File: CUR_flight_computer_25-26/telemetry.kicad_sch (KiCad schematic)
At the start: 10 parts, among them U4 Ai-Thinker-Ra-01, U9 E22-400M30S

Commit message: Update telemetry.kicad_sch
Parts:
- removed AE1: Antenna, symbol Device:Antenna
- removed C14: 100nF, symbol Device:C_Small
- removed C15: 10uF, symbol Device:C_Small
- removed C17, C18: C_Small, symbol Device:C_Small
- removed D1: D_Zener, symbol Device:D_Zener
- removed R7: 0, symbol Device:R_Small_US
- removed R8: 10k, symbol Device:R_Small_US
- removed U4: Ai-Thinker-Ra-01, RF_Module:Ai-Thinker-Ra-01-LoRa, symbol RF_Module:Ai-Thinker-Ra-01
- added AE2: Antenna, symbol Device:Antenna
- added C33: 1u, symbol Device:C_Small
- added C35, C36: C_Small, symbol Device:C_Small
- added R42: 0, symbol Device:R_Small_US
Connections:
- net VCC is gone; now on net +3V3: U9.10 (VCC), U9.9 (VCC)
- net +3V3: now also C33.1
- net GND: now also C33.2, C35.2, C36.2
- net RF_BUSY: now also U9.14 (BUSY)
- net RF_IO1: now also U9.13 (DIO1)
- net RF_IO2: now also U9.8 (DIO2)
- net RF_MISO: now also U9.16 (MISO)
- net RF_MOSI: now also U9.17 (MOSI)
- net RF_RXEN: now also U9.6 (RXEN)
- net RF_SCK: now also U9.18 (SCK)
- net RF_TXEN: now also U9.7 (TXEN)
- net ~{RF_NSS}: now also U9.19 (NSS)
- net ~{RF_RESET}: now also U9.15 (NRST)
- net at U9.21 (ANT): now also C35.1, R42.2
- new net: AE2.1 (A), C36.1, R42.1
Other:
- note added: "DIO1 - interrupt DIO2 - tx switch"
- note added: "Pick capacitor values to PI match antenna - leave to test later - do not place in BOM"
- note removed: "Pick capacitor values to PI match antenna - leave to test later"
- note removed: "use df2s5m4sl from toshiba"
- moved on the sheet: U9

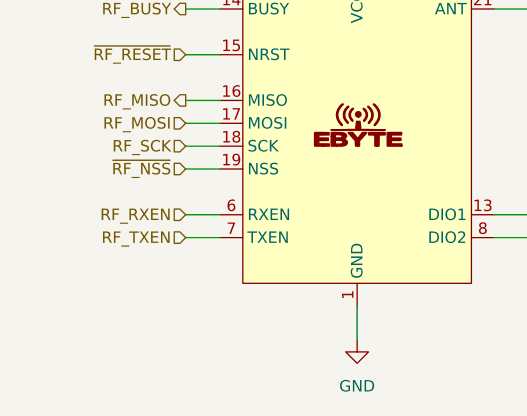
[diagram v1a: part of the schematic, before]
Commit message: updated pinout
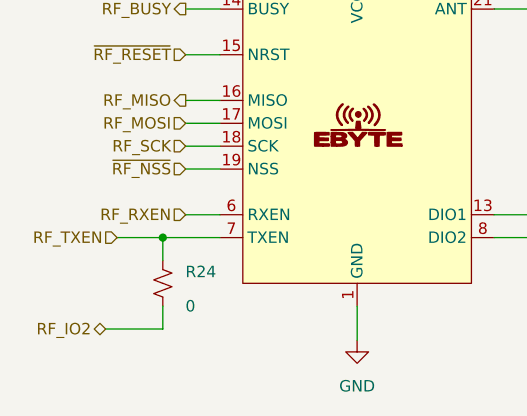
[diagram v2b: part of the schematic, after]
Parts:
- added R24: 0, symbol Device:R_Small_US
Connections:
- net RF_IO2: now also R24.2
- net RF_TXEN: now also R24.1
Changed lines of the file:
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@@
+	)
+	(junction
+		(at 27.94 71.12)
+		(diameter 0)
+		(color 0 0 0 0)
 	)
 	(junction
@@
 	(wire
 		(pts
-			(xy 30.48 71.12) (xy 34.29 71.12)
-		)
-		(stroke
-			(width 0)
-			(type default)
-		)
-	)
-	(wire
-		(pts
 			(xy 49.53 78.74) (xy 49.53 82.55)
 		)
@@
 	(wire
 		(pts
+			(xy 27.94 71.12) (xy 34.29 71.12)
+		)
+		(stroke
+			(width 0)
+			(type default)
+		)
+	)
+	(wire
+		(pts
+			(xy 22.86 71.12) (xy 27.94 71.12)
+		)
+		(stroke
+			(width 0)
+			(type default)
+		)
+	)
+	(wire
+		(pts
+			(xy 27.94 73.66) (xy 27.94 71.12)
+		)
+		(stroke
+			(width 0)
+			(type default)
+		)
+	)
+	(wire
+		(pts
 			(xy 68.58 68.58) (xy 64.77 68.58)
 		)
@@
 	(wire
 		(pts
+			(xy 27.94 78.74) (xy 27.94 81.28)
+		)
+		(stroke
+			(width 0)
+			(type default)
+		)
+	)
+	(wire
+		(pts
 			(xy 30.48 50.8) (xy 34.29 50.8)
+		)
+		(stroke
+			(width 0)
+			(type default)
+		)
+	)
+	(wire
+		(pts
+			(xy 21.59 81.28) (xy 27.94 81.28)
 		)
 		(stroke
@@
 		)
 	)
+	(hierarchical_label "RF_IO2"
+		(shape bidirectional)
+		(at 21.59 81.28 180)
+		(effects
+			(font
+				(size 1.27 1.27)
+			)
+			(justify right)
+		)
+	)
 	(hierarchical_label "RF_BUSY"
 		(shape output)
@@
 	(hierarchical_label "RF_TXEN"
 		(shape input)
-		(at 30.48 71.12 180)
+		(at 22.86 71.12 180)
 		(effects
 			(font
@@
 					(unit 1)
 				)
+			)
+		)
+	)
+	(symbol
+		(lib_id "Device:R_Small_US")
+		(at 27.94 76.2 0)
+		(unit 1)
+		(exclude_from_sim no)
+		(in_bom yes)
+		(on_board yes)
+		(dnp no)
+		(property "Reference" "R24"
+			(at 30.4529 74.9299 0)
+			(effects
+				(font
+					(size 1.27 1.27)
+				)
+				(justify left)
+			)
+		)
+		(property "Value" "0"
+			(at 30.4529 78.7399 0)
+			(effects
+				(font
+					(size 1.27 1.27)
+				)
+				(justify left)
+			)
+		)
+		(property "Footprint" ""
+			(at 27.94 76.2 0)
+			(effects
+				(font
+					(size 1.27 1.27)
+				)
+				(hide yes)
+			)
+		)
+		(property "Datasheet" "~"
+			(at 27.94 76.2 0)
+			(effects
+				(font
+					(size 1.27 1.27)
+				)
+				(hide yes)
+			)
+		)
+		(property "Description" "Resistor, small US symbol"
+			(at 27.94 76.2 0)
+			(effects
+				(font
+					(size 1.27 1.27)
+				)
+				(hide yes)
+			)
+		)
+		(pin "1"
+		)
+		(pin "2"
+		)
+		(instances
+			(project "CUR_flight_computer_25-26"
+				(path "/bf7761cc-1b32-4d86-809c-5f027005229b/16b7f3d3-745f-44d9-93a4-41f5bfd830cb"
+					(reference "R24")
+					(unit 1)
+				)

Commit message: updated all needed fixes
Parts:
- added R7: 10k, symbol Device:R_Small_US
- renumbered AE2 to AE1, C33 to C25, C35 to C26, C36 to C27, R24 to R8, R42 to R9, U9 to U5
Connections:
- net ~{RF_NSS}: now also R7.2
- new net +3.3V: R7.1
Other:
- note added: "Just in case something weird is happening here"
- moved on the sheet: AE1, C25, C26, C27, R8, R9, U5

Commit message: assigned footrpint
need to double check:
- HSE
- Capacitors

for some unknown reason cur kicad library refuses to work
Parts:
- C25, C26, C27: footprint (none) -> Capacitor_SMD:C_0603_1608Metric
- R7, R8, R9: footprint (none) -> Resistor_SMD:R_0603_1608Metric
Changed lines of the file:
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@@
 			)
 		)
-		(property "Footprint" ""
+		(property "Footprint" "Resistor_SMD:R_0603_1608Metric"
 			(at 59.69 76.2 0)
 			(effects
@@
 			)
 		)
-		(property "Footprint" ""
+		(property "Footprint" "Capacitor_SMD:C_0603_1608Metric"
 			(at 72.39 31.75 0)
 			(effects
@@
 			)
 		)
-		(property "Footprint" ""
+		(property "Footprint" "Capacitor_SMD:C_0603_1608Metric"
 			(at 102.87 49.53 0)
 			(effects
@@
 			)
 		)
-		(property "Footprint" ""
+		(property "Footprint" "Capacitor_SMD:C_0603_1608Metric"
 			(at 116.84 49.53 0)
 			(effects
@@
 			)
 		)
-		(property "Footprint" ""
+		(property "Footprint" "Resistor_SMD:R_0603_1608Metric"
 			(at 110.49 45.72 0)
 			(effects
@@
 			)
 		)
-		(property "Footprint" ""
+		(property "Footprint" "Resistor_SMD:R_0603_1608Metric"
 			(at 44.45 58.42 0)
 			(effects

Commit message: updated a couple footprints
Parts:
- removed AE1: Antenna, symbol Device:Antenna
- added J14: Conn_Coaxial_Small, symbol Connector:Conn_Coaxial_Small
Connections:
- net GND: now also J14.2 (Ext)
- net at C27.1, R9.1: now also J14.1 (In)
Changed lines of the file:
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@@
+	(wire
+		(pts
+			(xy 133.35 45.72) (xy 133.35 52.07)
+		)
+		(stroke
+			(width 0)
+			(type default)
+		)
+	)
 	(wire
 		(pts
@@
 	(wire
 		(pts
+			(xy 130.81 45.72) (xy 133.35 45.72)
+		)
+		(stroke
+			(width 0)
+			(type default)
+		)
+	)
+	(wire
+		(pts
 			(xy 40.64 63.5) (xy 44.45 63.5)
 		)
@@
 		(pts
 			(xy 44.45 52.07) (xy 44.45 55.88)
-		)
-		(stroke
-			(width 0)
-			(type default)
-		)
-	)
-	(wire
-		(pts
-			(xy 125.73 41.91) (xy 125.73 45.72)
 		)
 		(stroke
@@
 	)
 	(symbol
-		(lib_id "Device:Antenna")
-		(at 125.73 36.83 0)
-		(unit 1)
-		(exclude_from_sim no)
-		(in_bom yes)
-		(on_board yes)
-		(dnp no)
-		(fields_autoplaced yes)
-		(property "Reference" "AE1"
-			(at 128.27 36.1949 0)
-			(effects
-				(font
-					(size 1.27 1.27)
-				)
-				(justify left)
-			)
-		)
-		(property "Value" "Antenna"
-			(at 128.27 38.7349 0)
-			(effects
-				(font
-					(size 1.27 1.27)
-				)
-				(justify left)
-			)
-		)
-		(property "Footprint" ""
-			(at 125.73 36.83 0)
-			(effects
-				(font
-					(size 1.27 1.27)
-				)
-				(hide yes)
-			)
-		)
-		(property "Datasheet" "~"
-			(at 125.73 36.83 0)
-			(effects
-				(font
-					(size 1.27 1.27)
-				)
-				(hide yes)
-			)
-		)
-		(property "Description" "Antenna"
-			(at 125.73 36.83 0)
-			(effects
-				(font
-					(size 1.27 1.27)
-				)
-				(hide yes)
-			)
-		)
-		(pin "1"
-		)
-		(instances
-			(project "CUR_flight_computer_25-26"
-				(path "/bf7761cc-1b32-4d86-809c-5f027005229b/16b7f3d3-745f-44d9-93a4-41f5bfd830cb"
-					(reference "AE1")
-					(unit 1)
-				)
-			)
-		)
-	)
-	(symbol
 		(lib_id "power:GND")
 		(at 102.87 52.07 0)
@@
 	)
 	(symbol
+		(lib_id "Connector:Conn_Coaxial_Small")
+		(at 128.27 45.72 0)
+		(unit 1)
+		(exclude_from_sim no)
+		(in_bom yes)
+		(on_board yes)
+		(dnp no)
+		(fields_autoplaced yes)
+		(property "Reference" "J14"
+			(at 127.7504 39.37 0)
+			(effects
+				(font
+					(size 1.27 1.27)
+				)
+			)
+		)
+		(property "Value" "Conn_Coaxial_Small"
+			(at 127.7504 41.91 0)
+			(effects
+				(font
+					(size 1.27 1.27)
+				)
+			)
+		)
+		(property "Footprint" ""
+			(at 128.27 45.72 0)
+			(effects
+				(font
+					(size 1.27 1.27)
+				)
+				(hide yes)
+			)
+		)
+		(property "Datasheet" "~"
+			(at 128.27 45.72 0)
+			(effects
+				(font
+					(size 1.27 1.27)
+				)
+				(hide yes)
+			)
+		)
+		(property "Description" "small coaxial connector (BNC, SMA, SMB, SMC, Cinch/RCA, LEMO, ...)"
+			(at 128.27 45.72 0)
+			(effects
+				(font
+					(size 1.27 1.27)
+				)
+				(hide yes)
+			)
+		)
+		(pin "2"
+		)
+		(pin "1"
+		)
+		(instances
+			(project ""
+				(path "/bf7761cc-1b32-4d86-809c-5f027005229b/16b7f3d3-745f-44d9-93a4-41f5bfd830cb"
+					(reference "J14")
+					(unit 1)
+				)
+			)
+		)
+	)
+	(symbol
 		(lib_id "Device:C_Small")
 		(at 116.84 49.53 0)
@@
 					(unit 1)
 				)
+			)
+		)
+	)
+	(symbol
+		(lib_id "power:GND")
+		(at 133.35 52.07 0)
+		(unit 1)
+		(exclude_from_sim no)
+		(in_bom yes)
+		(on_board yes)
+		(dnp no)
+		(fields_autoplaced yes)
+		(property "Reference" "#PWR0113"
+			(at 133.35 58.42 0)
+			(effects
+				(font
+					(size 1.27 1.27)
+				)
+				(hide yes)
+			)
+		)
+		(property "Value" "GND"
+			(at 133.35 57.15 0)
+			(effects
+				(font
+					(size 1.27 1.27)
+				)
+			)
+		)
+		(property "Footprint" ""
+			(at 133.35 52.07 0)
+			(effects
+				(font
+					(size 1.27 1.27)
+				)
+				(hide yes)
+			)
+		)
+		(property "Datasheet" ""
+			(at 133.35 52.07 0)
+			(effects
+				(font
+					(size 1.27 1.27)
+				)
+				(hide yes)
+			)
+		)
+		(property "Description" "Power symbol creates a global label with name \"GND\" , ground"
+			(at 133.35 52.07 0)
+			(effects
+				(font
+					(size 1.27 1.27)
+				)
+				(hide yes)
+			)
+		)
+		(pin "1"
+		)
+		(instances
+			(project "CUR_flight_computer_25-26"
+				(path "/bf7761cc-1b32-4d86-809c-5f027005229b/16b7f3d3-745f-44d9-93a4-41f5bfd830cb"
+					(reference "#PWR0113")
+					(unit 1)
+				)

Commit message: Revert "updated a couple footprints"
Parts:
- removed J14: Conn_Coaxial_Small, symbol Connector:Conn_Coaxial_Small
- added AE1: Antenna, symbol Device:Antenna
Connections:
- net at C27.1, R9.1: now also AE1.1 (A)
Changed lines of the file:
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@@
-	(wire
-		(pts
-			(xy 133.35 45.72) (xy 133.35 52.07)
-		)
-		(stroke
-			(width 0)
-			(type default)
-		)
-	)
 	(wire
 		(pts
@@
 	(wire
 		(pts
-			(xy 130.81 45.72) (xy 133.35 45.72)
-		)
-		(stroke
-			(width 0)
-			(type default)
-		)
-	)
-	(wire
-		(pts
 			(xy 40.64 63.5) (xy 44.45 63.5)
 		)
@@
 		(pts
 			(xy 44.45 52.07) (xy 44.45 55.88)
+		)
+		(stroke
+			(width 0)
+			(type default)
+		)
+	)
+	(wire
+		(pts
+			(xy 125.73 41.91) (xy 125.73 45.72)
 		)
 		(stroke
@@
 	)
 	(symbol
+		(lib_id "Device:Antenna")
+		(at 125.73 36.83 0)
+		(unit 1)
+		(exclude_from_sim no)
+		(in_bom yes)
+		(on_board yes)
+		(dnp no)
+		(fields_autoplaced yes)
+		(property "Reference" "AE1"
+			(at 128.27 36.1949 0)
+			(effects
+				(font
+					(size 1.27 1.27)
+				)
+				(justify left)
+			)
+		)
+		(property "Value" "Antenna"
+			(at 128.27 38.7349 0)
+			(effects
+				(font
+					(size 1.27 1.27)
+				)
+				(justify left)
+			)
+		)
+		(property "Footprint" ""
+			(at 125.73 36.83 0)
+			(effects
+				(font
+					(size 1.27 1.27)
+				)
+				(hide yes)
+			)
+		)
+		(property "Datasheet" "~"
+			(at 125.73 36.83 0)
+			(effects
+				(font
+					(size 1.27 1.27)
+				)
+				(hide yes)
+			)
+		)
+		(property "Description" "Antenna"
+			(at 125.73 36.83 0)
+			(effects
+				(font
+					(size 1.27 1.27)
+				)
+				(hide yes)
+			)
+		)
+		(pin "1"
+		)
+		(instances
+			(project "CUR_flight_computer_25-26"
+				(path "/bf7761cc-1b32-4d86-809c-5f027005229b/16b7f3d3-745f-44d9-93a4-41f5bfd830cb"
+					(reference "AE1")
+					(unit 1)
+				)
+			)
+		)
+	)
+	(symbol
 		(lib_id "power:GND")
 		(at 102.87 52.07 0)
@@
 	)
 	(symbol
-		(lib_id "Connector:Conn_Coaxial_Small")
-		(at 128.27 45.72 0)
-		(unit 1)
-		(exclude_from_sim no)
-		(in_bom yes)
-		(on_board yes)
-		(dnp no)
-		(fields_autoplaced yes)
-		(property "Reference" "J14"
-			(at 127.7504 39.37 0)
-			(effects
-				(font
-					(size 1.27 1.27)
-				)
-			)
-		)
-		(property "Value" "Conn_Coaxial_Small"
-			(at 127.7504 41.91 0)
-			(effects
-				(font
-					(size 1.27 1.27)
-				)
-			)
-		)
-		(property "Footprint" ""
-			(at 128.27 45.72 0)
-			(effects
-				(font
-					(size 1.27 1.27)
-				)
-				(hide yes)
-			)
-		)
-		(property "Datasheet" "~"
-			(at 128.27 45.72 0)
-			(effects
-				(font
-					(size 1.27 1.27)
-				)
-				(hide yes)
-			)
-		)
-		(property "Description" "small coaxial connector (BNC, SMA, SMB, SMC, Cinch/RCA, LEMO, ...)"
-			(at 128.27 45.72 0)
-			(effects
-				(font
-					(size 1.27 1.27)
-				)
-				(hide yes)
-			)
-		)
-		(pin "2"
-		)
-		(pin "1"
-		)
-		(instances
-			(project ""
-				(path "/bf7761cc-1b32-4d86-809c-5f027005229b/16b7f3d3-745f-44d9-93a4-41f5bfd830cb"
-					(reference "J14")
-					(unit 1)
-				)
-			)
-		)
-	)
-	(symbol
 		(lib_id "Device:C_Small")
 		(at 116.84 49.53 0)
@@
 					(unit 1)
 				)
-			)
-		)
-	)
-	(symbol
-		(lib_id "power:GND")
-		(at 133.35 52.07 0)
-		(unit 1)
-		(exclude_from_sim no)
-		(in_bom yes)
-		(on_board yes)
-		(dnp no)
-		(fields_autoplaced yes)
-		(property "Reference" "#PWR0113"
-			(at 133.35 58.42 0)
-			(effects
-				(font
-					(size 1.27 1.27)
-				)
-				(hide yes)
-			)
-		)
-		(property "Value" "GND"
-			(at 133.35 57.15 0)
-			(effects
-				(font
-					(size 1.27 1.27)
-				)
-			)
-		)
-		(property "Footprint" ""
-			(at 133.35 52.07 0)
-			(effects
-				(font
-					(size 1.27 1.27)
-				)
-				(hide yes)
-			)
-		)
-		(property "Datasheet" ""
-			(at 133.35 52.07 0)
-			(effects
-				(font
-					(size 1.27 1.27)
-				)
-				(hide yes)
-			)
-		)
-		(property "Description" "Power symbol creates a global label with name \"GND\" , ground"
-			(at 133.35 52.07 0)
-			(effects
-				(font
-					(size 1.27 1.27)
-				)
-				(hide yes)
-			)
-		)
-		(pin "1"
-		)
-		(instances
-			(project "CUR_flight_computer_25-26"
-				(path "/bf7761cc-1b32-4d86-809c-5f027005229b/16b7f3d3-745f-44d9-93a4-41f5bfd830cb"
-					(reference "#PWR0113")
-					(unit 1)
-				)

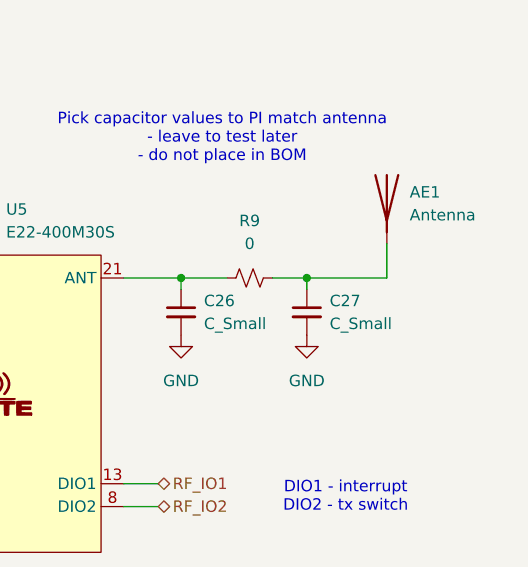
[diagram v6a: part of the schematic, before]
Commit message: changed footprints
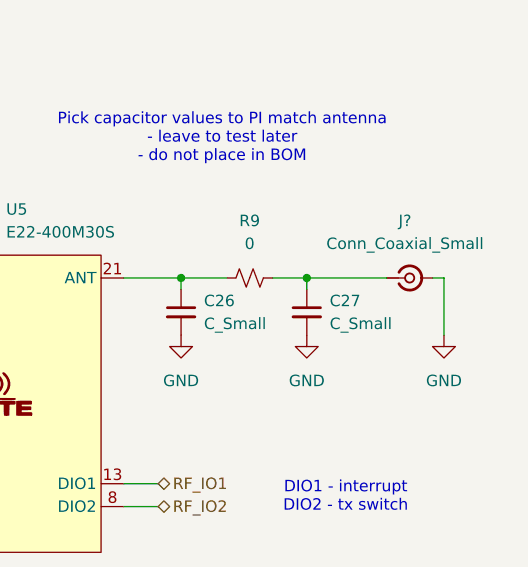
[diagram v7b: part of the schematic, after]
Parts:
- removed AE1: Antenna, symbol Device:Antenna
- added J?: Conn_Coaxial_Small, symbol Connector:Conn_Coaxial_Small
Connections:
- net GND: now also J?.2 (Ext)
- net at C27.1, R9.1: now also J?.1 (In)
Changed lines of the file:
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@@
+	(wire
+		(pts
+			(xy 132.08 45.72) (xy 132.08 52.07)
+		)
+		(stroke
+			(width 0)
+			(type default)
+		)
+	)
 	(wire
 		(pts
@@
 	(wire
 		(pts
+			(xy 130.81 45.72) (xy 132.08 45.72)
+		)
+		(stroke
+			(width 0)
+			(type default)
+		)
+	)
+	(wire
+		(pts
 			(xy 53.34 81.28) (xy 59.69 81.28)
 		)
@@
 		(pts
 			(xy 44.45 52.07) (xy 44.45 55.88)
-		)
-		(stroke
-			(width 0)
-			(type default)
-		)
-	)
-	(wire
-		(pts
-			(xy 125.73 41.91) (xy 125.73 45.72)
 		)
 		(stroke
@@
 	)
 	(symbol
-		(lib_id "Device:Antenna")
-		(at 125.73 36.83 0)
-		(unit 1)
-		(exclude_from_sim no)
-		(in_bom yes)
-		(on_board yes)
-		(dnp no)
-		(fields_autoplaced yes)
-		(property "Reference" "AE1"
-			(at 128.27 36.1949 0)
-			(effects
-				(font
-					(size 1.27 1.27)
-				)
-				(justify left)
-			)
-		)
-		(property "Value" "Antenna"
-			(at 128.27 38.7349 0)
-			(effects
-				(font
-					(size 1.27 1.27)
-				)
-				(justify left)
-			)
-		)
-		(property "Footprint" ""
-			(at 125.73 36.83 0)
-			(effects
-				(font
-					(size 1.27 1.27)
-				)
-				(hide yes)
-			)
-		)
-		(property "Datasheet" "~"
-			(at 125.73 36.83 0)
-			(effects
-				(font
-					(size 1.27 1.27)
-				)
-				(hide yes)
-			)
-		)
-		(property "Description" "Antenna"
-			(at 125.73 36.83 0)
-			(effects
-				(font
-					(size 1.27 1.27)
-				)
-				(hide yes)
-			)
-		)
-		(pin "1"
-		)
-		(instances
-			(project "CUR_flight_computer_25-26"
-				(path "/bf7761cc-1b32-4d86-809c-5f027005229b/16b7f3d3-745f-44d9-93a4-41f5bfd830cb"
-					(reference "AE1")
-					(unit 1)
-				)
-			)
-		)
-	)
-	(symbol
 		(lib_id "power:GND")
 		(at 102.87 52.07 0)
@@
 	)
 	(symbol
+		(lib_id "Connector:Conn_Coaxial_Small")
+		(at 128.27 45.72 0)
+		(unit 1)
+		(exclude_from_sim no)
+		(in_bom yes)
+		(on_board yes)
+		(dnp no)
+		(fields_autoplaced yes)
+		(property "Reference" "J?"
+			(at 127.7504 39.37 0)
+			(effects
+				(font
+					(size 1.27 1.27)
+				)
+			)
+		)
+		(property "Value" "Conn_Coaxial_Small"
+			(at 127.7504 41.91 0)
+			(effects
+				(font
+					(size 1.27 1.27)
+				)
+			)
+		)
+		(property "Footprint" ""
+			(at 128.27 45.72 0)
+			(effects
+				(font
+					(size 1.27 1.27)
+				)
+				(hide yes)
+			)
+		)
+		(property "Datasheet" "~"
+			(at 128.27 45.72 0)
+			(effects
+				(font
+					(size 1.27 1.27)
+				)
+				(hide yes)
+			)
+		)
+		(property "Description" "small coaxial connector (BNC, SMA, SMB, SMC, Cinch/RCA, LEMO, ...)"
+			(at 128.27 45.72 0)
+			(effects
+				(font
+					(size 1.27 1.27)
+				)
+				(hide yes)
+			)
+		)
+		(pin "1"
+		)
+		(pin "2"
+		)
+		(instances
+			(project ""
+				(path "/bf7761cc-1b32-4d86-809c-5f027005229b/16b7f3d3-745f-44d9-93a4-41f5bfd830cb"
+					(reference "J?")
+					(unit 1)
+				)
+			)
+		)
+	)
+	(symbol
 		(lib_id "power:+3V3")
 		(at 66.04 22.86 0)
@@
 					(unit 1)
 				)
+			)
+		)
+	)
+	(symbol
+		(lib_id "power:GND")
+		(at 132.08 52.07 0)
+		(unit 1)
+		(exclude_from_sim no)
+		(in_bom yes)
+		(on_board yes)
+		(dnp no)
+		(fields_autoplaced yes)
+		(property "Reference" "#PWR0113"
+			(at 132.08 58.42 0)
+			(effects
+				(font
+					(size 1.27 1.27)
+				)
+				(hide yes)
+			)
+		)
+		(property "Value" "GND"
+			(at 132.08 57.15 0)
+			(effects
+				(font
+					(size 1.27 1.27)
+				)
+			)
+		)
+		(property "Footprint" ""
+			(at 132.08 52.07 0)
+			(effects
+				(font
+					(size 1.27 1.27)
+				)
+				(hide yes)
+			)
+		)
+		(property "Datasheet" ""
+			(at 132.08 52.07 0)
+			(effects
+				(font
+					(size 1.27 1.27)
+				)
+				(hide yes)
+			)
+		)
+		(property "Description" "Power symbol creates a global label with name \"GND\" , ground"
+			(at 132.08 52.07 0)
+			(effects
+				(font
+					(size 1.27 1.27)
+				)
+				(hide yes)
+			)
+		)
+		(pin "1"
+		)
+		(instances
+			(project "CUR_flight_computer_25-26"
+				(path "/bf7761cc-1b32-4d86-809c-5f027005229b/16b7f3d3-745f-44d9-93a4-41f5bfd830cb"
+					(reference "#PWR0113")
+					(unit 1)
+				)

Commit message: Update telemetry.kicad_sch
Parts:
- gave numbers to parts that had none: 1
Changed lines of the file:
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@@
 		(dnp no)
 		(fields_autoplaced yes)
-		(property "Reference" "J?"
+		(property "Reference" "J14"
 			(at 127.7504 39.37 0)
 			(effects
@@
 			(project ""
 				(path "/bf7761cc-1b32-4d86-809c-5f027005229b/16b7f3d3-745f-44d9-93a4-41f5bfd830cb"
-					(reference "J?")
+					(reference "J14")
 					(unit 1)
 				)
